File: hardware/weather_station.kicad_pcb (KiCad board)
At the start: 4 copper layers, 59.7 x 27.6 mm, 77 parts, among them J1 USB_MICRO, P1 CONN_01X04, P2 CONN_01X04, P3 CONN_01X06, P4 CONN_01X04, P5 CONN_01X09, Q1 BD135, Q2 BD135, SW1 SWITCH_SPDT, U1 nRF51x22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

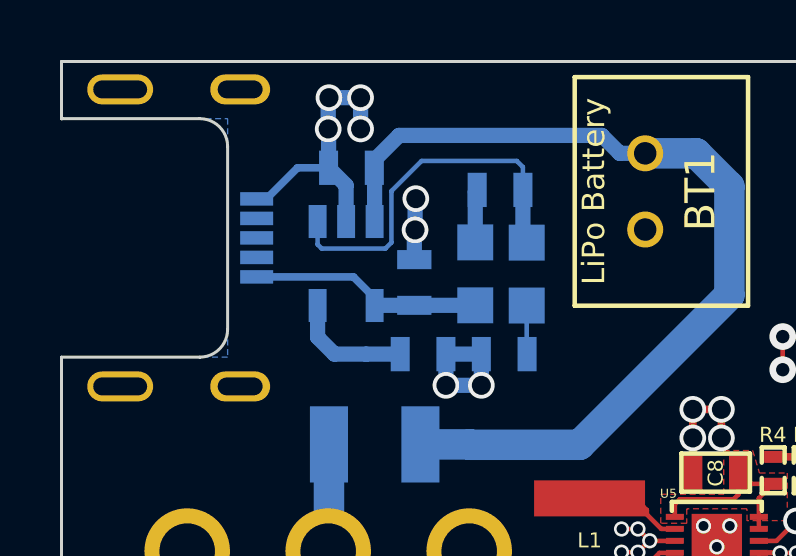
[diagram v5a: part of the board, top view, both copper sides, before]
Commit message: Add the weather logo footprint to the layout
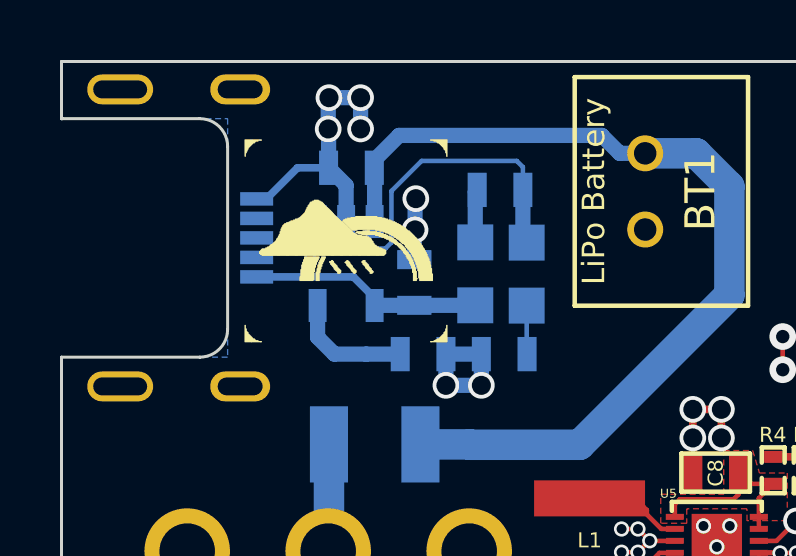
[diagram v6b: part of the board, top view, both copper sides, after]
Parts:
- added weather_logo: , weather:weather_logo, F.Cu at (167.3, 82.7)
